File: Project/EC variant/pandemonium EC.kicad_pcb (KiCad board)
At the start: 4 copper layers, 190.5 x 81.6 mm, 105 parts, among them J1 USB_C_Receptacle_USB2.0, SW1 DFU, U11 PRTR5V0U2X, U5 OPA354, U6 74HC4051, U7 74HC4051, U8 STM32F072CBT6, U9 XC6206PxxxMR-Regulator_Linear

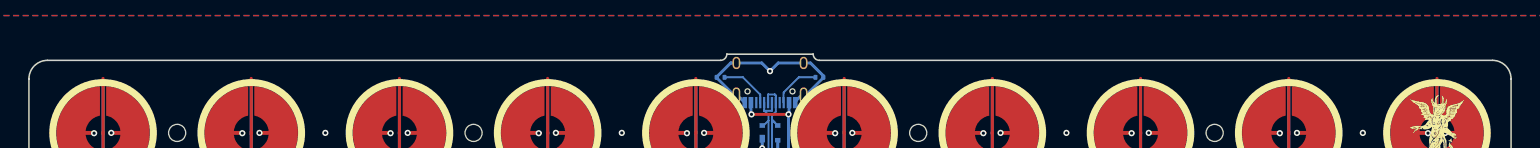
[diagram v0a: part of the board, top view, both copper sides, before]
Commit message: EC plates created
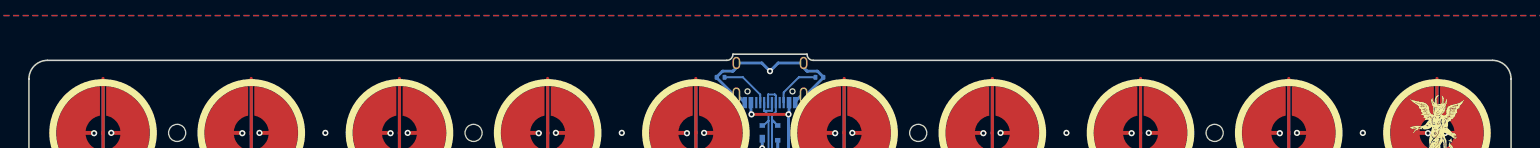
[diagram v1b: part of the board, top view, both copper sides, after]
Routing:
- net GND: track 71.3 -> 71.9 mm
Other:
- outline, holes or cut-outs redrawn
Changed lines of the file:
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@@
   (gr_arc (start 34.13125 104.775) (mid 32.447499 104.077516) (end 31.75 102.39375)
     (stroke (width 0.2) (type solid)) (layer "Edge.Cuts"))
-  (gr_line (start 132.55625 23.21875) (end 121.44375 23.21875)
+  (gr_line (start 131.7625 23.21875) (end 122.2375 23.21875)
     (stroke (width 0.2) (type default)) (layer "Edge.Cuts"))
   (gr_arc (start 222.25 102.39375) (mid 221.552508 104.077494) (end 219.86875 104.775)
     (stroke (width 0.2) (type solid)) (layer "Edge.Cuts"))
-  (gr_line (start 120.65 24.0125) (end 34.13125 24.0125)
-    (stroke (width 0.2) (type default)) (layer "Edge.Cuts"))
-  (gr_arc (start 133.35 24.0125) (mid 132.788719 23.780031) (end 132.55625 23.21875)
-    (stroke (width 0.2) (type default)) (layer "Edge.Cuts"))
-  (gr_arc (start 121.44375 23.21875) (mid 121.211251 23.780001) (end 120.65 24.0125)
+  (gr_line (start 121.44375 24.0125) (end 34.13125 24.0125)
+    (stroke (width 0.2) (type default)) (layer "Edge.Cuts"))
+  (gr_arc (start 132.55625 24.0125) (mid 131.994937 23.780048) (end 131.7625 23.21875)
+    (stroke (width 0.2) (type default)) (layer "Edge.Cuts"))
+  (gr_arc (start 122.2375 23.21875) (mid 122.005004 23.780019) (end 121.44375 24.0125)
     (stroke (width 0.2) (type default)) (layer "Edge.Cuts"))
   (gr_line (start 31.75 26.39375) (end 31.75 102.39375)
@@
   (gr_arc (start 219.868825 24.012425) (mid 221.552619 24.709896) (end 222.250075 26.393675)
     (stroke (width 0.2) (type solid)) (layer "Edge.Cuts"))
-  (gr_line (start 219.868825 24.012425) (end 133.35 24.0125)
+  (gr_line (start 219.868825 24.012425) (end 132.55625 24.0125)
     (stroke (width 0.2) (type default)) (layer "Edge.Cuts"))
   (gr_arc (start 31.75 26.39375) (mid 32.447475 24.709975) (end 34.13125 24.0125)
@@
   (segment (start 58.409681 75.269941) (end 57.94375 75.269941) (width 0.25) (layer "B.Cu") (net 8))
   (segment (start 56.35625 80.9625) (end 54.10625 83.2125) (width 0.25) (layer "B.Cu") (net 8))
-  (segment (start 132.201 24.35) (end 133.86 26.009) (width 0.381) (layer "B.Cu") (net 8))
   (segment (start 63.085811 81.215986) (end 63.974832 81.215986) (width 0.25) (layer "B.Cu") (net 8))
   (segment (start 57.10625 81.7125) (end 56.35625 80.9625) (width 0.25) (layer "B.Cu") (net 8))
@@
   (segment (start 133.86 26.19375) (end 133.86 26.236919) (width 0.381) (layer "B.Cu") (net 8))
   (segment (start 58.915 75.269941) (end 58.915 74.406068) (width 0.25) (layer "B.Cu") (net 8))
+  (segment (start 133.109419 25.4) (end 131.7625 25.4) (width 0.381) (layer "B.Cu") (net 8))
   (segment (start 125.95 24.35) (end 122.68 24.35) (width 0.381) (layer "B.Cu") (net 8))
   (segment (start 80.9625 90.20375) (end 80.9625 91.120322) (width 0.25) (layer "B.Cu") (net 8))
   (segment (start 61.9125 88.2625) (end 63.393254 88.2625) (width 0.25) (layer "B.Cu") (net 8))
+  (segment (start 122.2375 25.4) (end 122.68 24.9575) (width 0.381) (layer "B.Cu") (net 8))
   (segment (start 120.14 26.150581) (end 120.14 26.19375) (width 0.381) (layer "B.Cu") (net 8))
   (segment (start 173.0375 87.017749) (end 173.037499 87.017748) (width 0.25) (layer "B.Cu") (net 8))
@@
   (segment (start 167.1975 84.6625) (end 168.15875 84.6625) (width 0.25) (layer "B.Cu") (net 8))
   (segment (start 80.9625 86.28375) (end 80.008984 86.28375) (width 0.25) (layer "B.Cu") (net 8))
+  (segment (start 120.14 26.150581) (end 120.890581 25.4) (width 0.381) (layer "B.Cu") (net 8))
   (segment (start 51.990908 85.725) (end 51.994552 85.728644) (width 0.25) (layer "B.Cu") (net 8))
   (segment (start 58.2 88.2625) (end 59.1875 88.2625) (width 0.25) (layer "B.Cu") (net 8))
   (segment (start 84.93125 93.37875) (end 84.93125 94.356948) (width 0.25) (layer "B.Cu") (net 8))
+  (segment (start 131.7625 25.4) (end 131.32 24.9575) (width 0.381) (layer "B.Cu") (net 8))
   (segment (start 58.2 88.2625) (end 58.2 88.79625) (width 0.25) (layer "B.Cu") (net 8))
   (segment (start 56.35625 80.9625) (end 54.10625 78.7125) (width 0.25) (layer "B.Cu") (net 8))
   (segment (start 92.075 88.215) (end 92.075 87.3125) (width 0.25) (layer "B.Cu") (net 8))
-  (segment (start 131.32 24.35) (end 132.201 24.35) (width 0.381) (layer "B.Cu") (net 8))
   (segment (start 80.008984 86.28375) (end 80.006756 86.285978) (width 0.25) (layer "B.Cu") (net 8))
   (segment (start 169.06875 93.37875) (end 169.06875 94.45625) (width 0.25) (layer "B.Cu") (net 8))
@@
   (segment (start 54.10625 83.2125) (end 54.10625 85.125) (width 0.25) (layer "B.Cu") (net 8))
   (segment (start 54.10625 78.7125) (end 52.19375 78.7125) (width 0.25) (layer "B.Cu") (net 8))
+  (segment (start 122.68 24.9575) (end 122.68 24.35) (width 0.381) (layer "B.Cu") (net 8))
   (segment (start 58.60625 77.91875) (end 56.35625 80.16875) (width 0.25) (layer "B.Cu") (net 8))
   (segment (start 56.35625 80.16875) (end 56.35625 80.9625) (width 0.25) (layer "B.Cu") (net 8))
@@
   (segment (start 85.215 85.1275) (end 84.6175 85.725) (width 0.25) (layer "B.Cu") (net 8))
   (segment (start 122.433081 28.53) (end 122.68 28.53) (width 0.381) (layer "B.Cu") (net 8))
-  (segment (start 122.68 24.35) (end 121.940581 24.35) (width 0.381) (layer "B.Cu") (net 8))
   (segment (start 58.2 87.79875) (end 58.2 88.2625) (width 0.25) (layer "B.Cu") (net 8))
+  (segment (start 133.86 26.19375) (end 133.86 26.150581) (width 0.381) (layer "B.Cu") (net 8))
+  (segment (start 131.32 24.9575) (end 131.32 24.35) (width 0.381) (layer "B.Cu") (net 8))
   (segment (start 58.915 75.269941) (end 58.409681 75.269941) (width 0.25) (layer "B.Cu") (net 8))
   (segment (start 60.51875 81.7125) (end 57.10625 81.7125) (width 0.25) (layer "B.Cu") (net 8))
   (segment (start 122.835 28.53) (end 123.75 29.445) (width 0.381) (layer "B.Cu") (net 8))
   (segment (start 120.14 26.19375) (end 120.14 26.236919) (width 0.381) (layer "B.Cu") (net 8))
+  (segment (start 133.86 26.150581) (end 133.109419 25.4) (width 0.381) (layer "B.Cu") (net 8))
   (segment (start 84.93125 94.356948) (end 84.926318 94.36188) (width 0.25) (layer "B.Cu") (net 8))
-  (segment (start 121.940581 24.35) (end 120.14 26.150581) (width 0.381) (layer "B.Cu") (net 8))
   (segment (start 127 25.4) (end 125.95 24.35) (width 0.381) (layer "B.Cu") (net 8))
   (segment (start 51.990908 76.148536) (end 51.990908 75.15831) (width 0.25) (layer "B.Cu") (net 8))
   (segment (start 63.96826 83.178076) (end 63.980049 83.166287) (width 0.25) (layer "B.Cu") (net 8))
-  (segment (start 133.86 26.009) (end 133.86 26.19375) (width 0.381) (layer "B.Cu") (net 8))
   (segment (start 63.393254 88.2625) (end 63.401824 88.25393) (width 0.25) (layer "B.Cu") (net 8))
+  (segment (start 120.890581 25.4) (end 122.2375 25.4) (width 0.381) (layer "B.Cu") (net 8))
   (segment (start 51.994552 85.728644) (end 51.994552 86.682577) (width 0.25) (layer "B.Cu") (net 8))
   (via (at 99.4798 52.387499) (size 0.8) (drill 0.4) (layers "F.Cu" "B.Cu") (net 9))
